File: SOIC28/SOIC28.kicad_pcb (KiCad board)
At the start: 2 copper layers, 23.1 x 35.8 mm, 7 parts, among them J1 Conn_01x14, J2 Conn_02x14_Counter_Clockwise, J3 Conn_01x14, J4 Conn_02x14_Counter_Clockwise

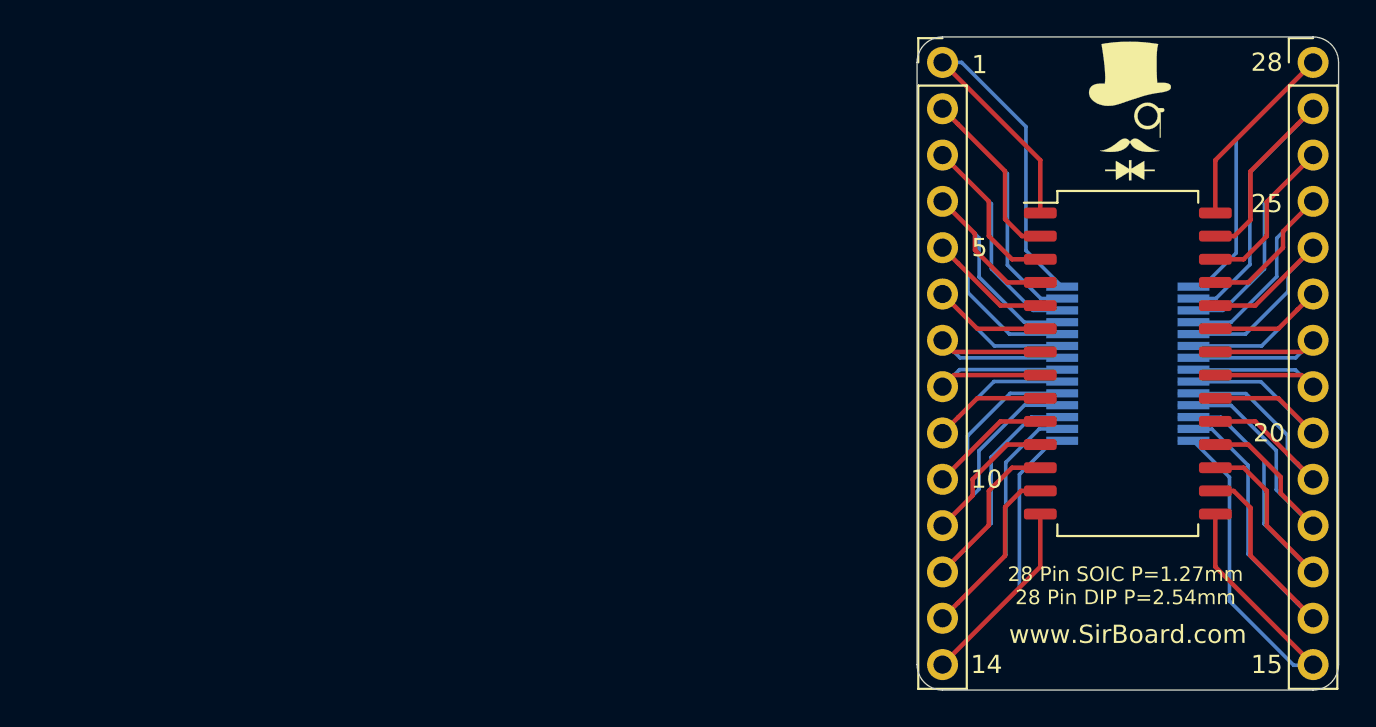
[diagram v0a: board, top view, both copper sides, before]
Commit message: Silkscreens and sizes updated
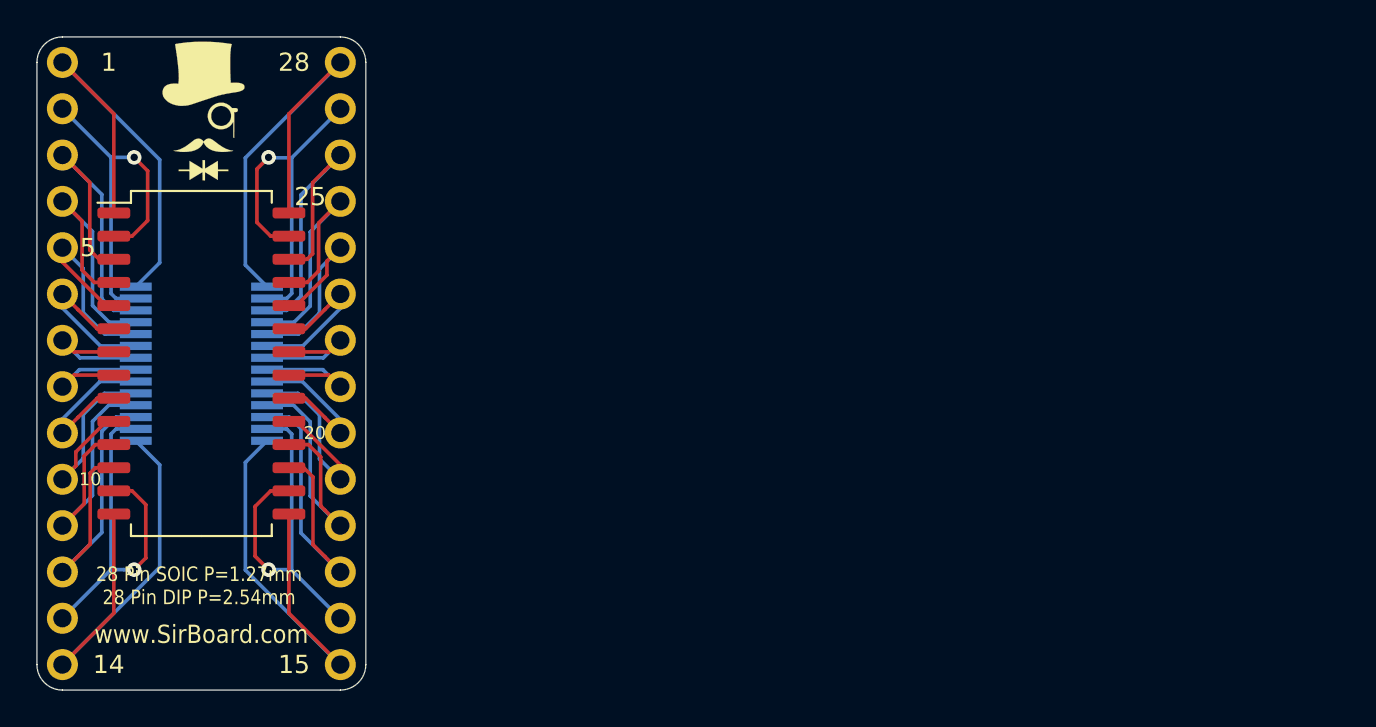
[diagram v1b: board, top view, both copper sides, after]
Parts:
- J1, J3: moved to B.Cu
- moved J3 53.3 mm to (154.9, 105.4), turned to 180 degrees
- moved G*** 50.8 mm to (147.3, 113.7)
- moved G*** 50.8 mm to (147.4, 108.1)
- moved G*** 50.8 mm to (147.3, 133.7)
- moved J2 50.8 mm to (147.3, 121.9)
- moved J4 50.8 mm to (147.3, 121.9)
- moved J1 48.3 mm to (139.7, 105.4), turned to 180 degrees
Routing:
- net Net-(J2-Pad22): track 13.3 -> 7.49 mm
- net Net-(J2-Pad21): track 13.3 -> 7.50 mm
- net Net-(J1-Pad7): track 13.3 -> 7.50 mm
- net Net-(J1-Pad8): track 13.3 -> 7.49 mm
- net Net-(J2-Pad20): track 14.6 -> 9.26 mm
- net Net-(J2-Pad23): track 14.6 -> 9.24 mm
- net Net-(J1-Pad9): track 14.6 -> 9.24 mm
- net Net-(J1-Pad6): track 14.6 -> 9.26 mm
- net Net-(J2-Pad19): track 16.6 -> 12.0 mm
- net Net-(J1-Pad5): track 16.6 -> 12.0 mm
- net Net-(J1-Pad13): track 24.4 -> 19.8 mm, vias 0 -> 1
- net Net-(J2-Pad24): track 16.5 -> 12.0 mm
- net Net-(J1-Pad10): track 16.5 -> 12.0 mm
- net Net-(J2-Pad27): track 24.4 -> 19.9 mm, vias 0 -> 1
- net Net-(J1-Pad2): track 24.4 -> 19.9 mm, vias 0 -> 1
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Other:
- board size 23.1 x 35.8 mm -> 18 x 35.8 mm

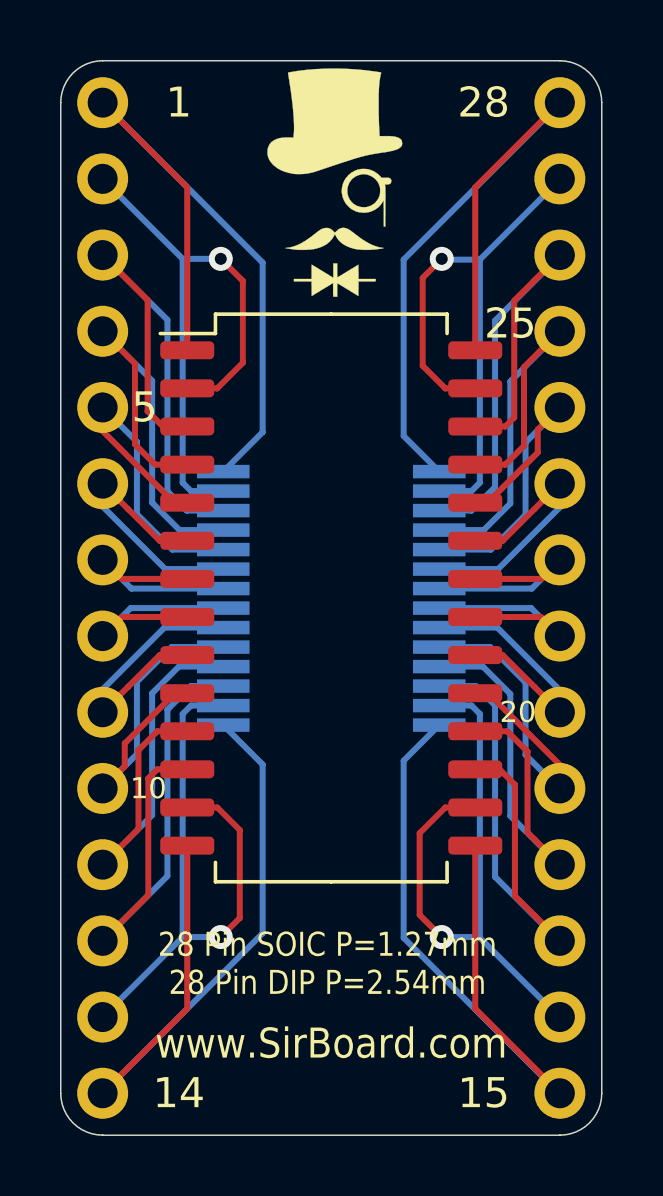
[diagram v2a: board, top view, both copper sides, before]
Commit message: Pin Numbering edited
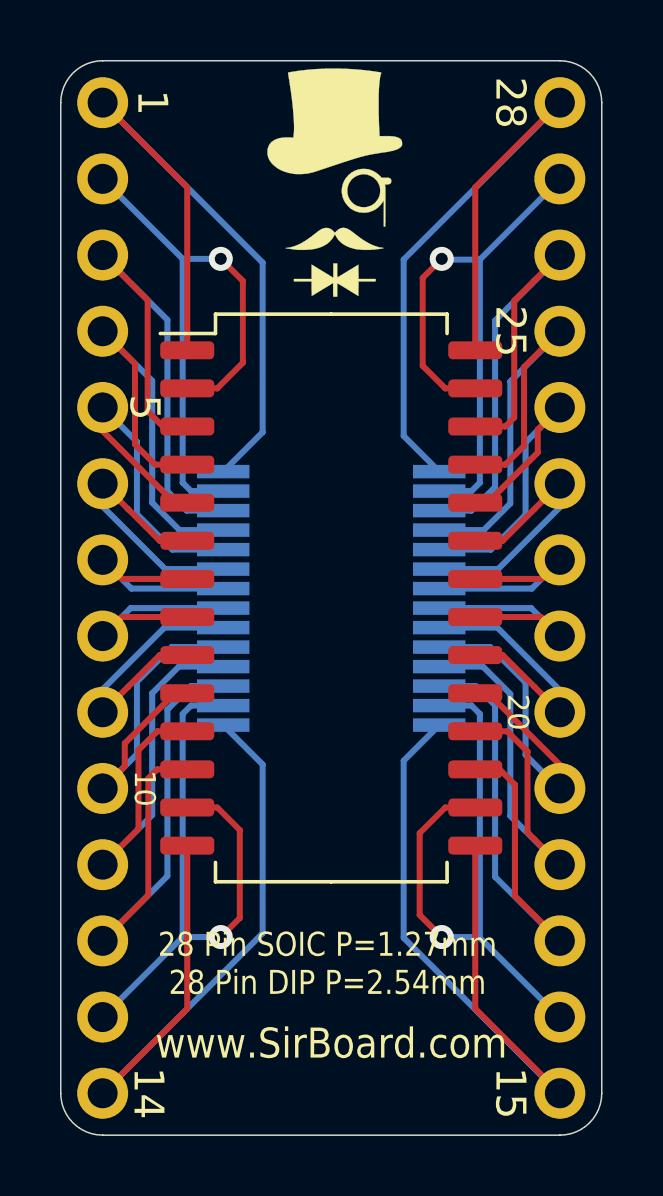
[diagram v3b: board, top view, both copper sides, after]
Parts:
- J1, J3: moved to F.Cu
- turned J1 to 0 degrees
- turned J3 to 0 degrees

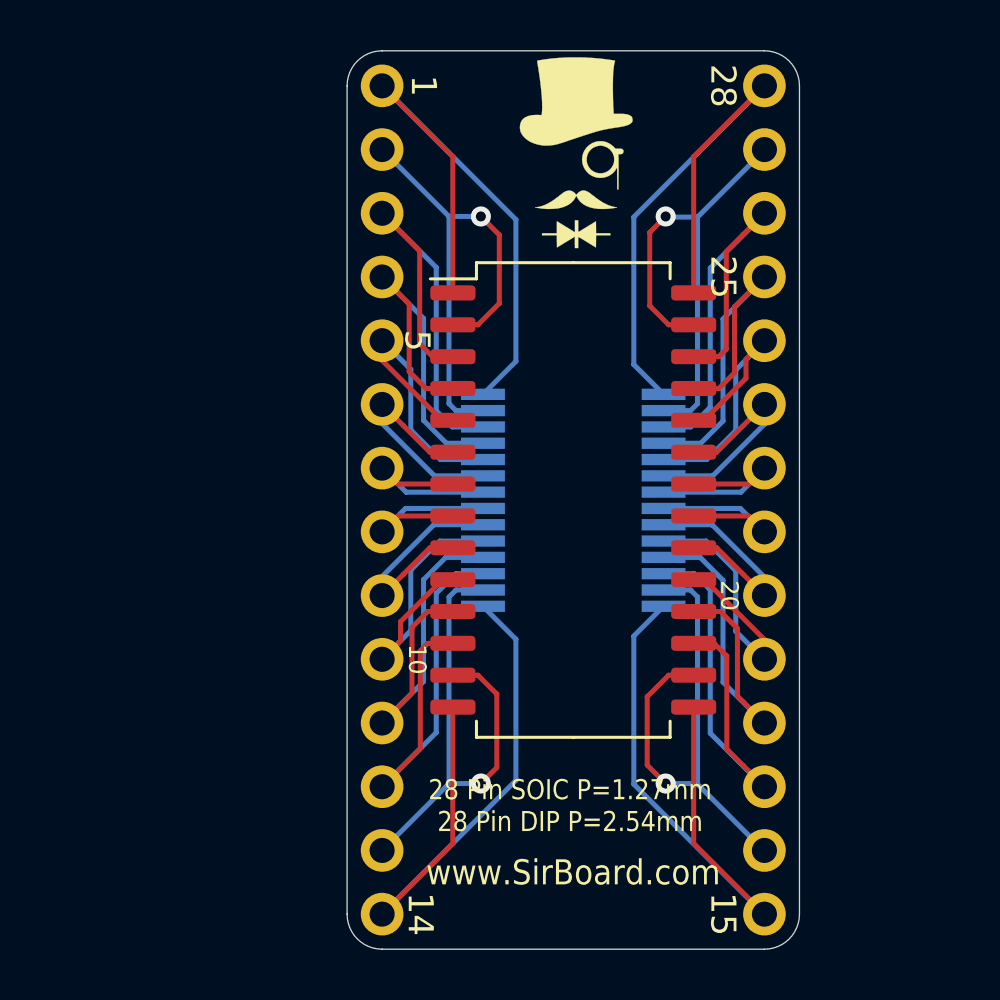
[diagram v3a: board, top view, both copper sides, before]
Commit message: Numbering Orientation Edited
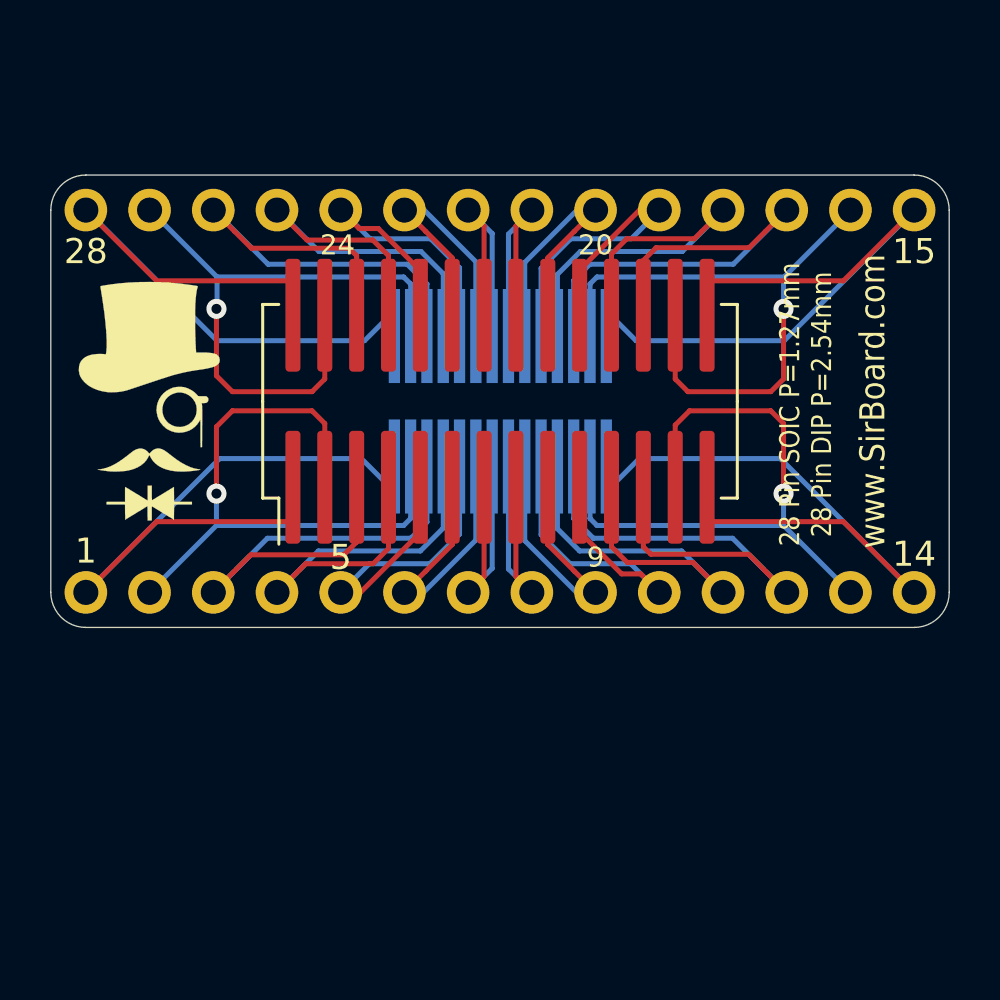
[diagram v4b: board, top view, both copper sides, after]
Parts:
- removed the G*** at (147.4, 108.1)
- removed the G*** at (147.3, 133.7)
- added G***: LOGO, logo:logo94x134, B.Cu at (157.2, 118.0)
- added G***: LOGO, logo:logo94x134, F.Cu at (130.4, 118.0)
- J1, J3: moved to B.Cu
- moved J3 27.5 mm to (127.9, 110.4), turned to 270 degrees
- moved J1 23.4 mm to (127.9, 125.6), turned to 270 degrees
- moved G*** 12.0 mm to (136.1, 118.0), turned to 90 degrees
- moved J4 4.90 mm to (144.4, 118.0), turned to 90 degrees
- moved J2 4.90 mm to (144.4, 118.0), turned to 90 degrees
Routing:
- net Net-(J1-Pad13): track 19.8 -> 25.4 mm
- net Net-(J2-Pad27): track 19.9 -> 25.3 mm
- net Net-(J2-Pad16): track 20.0 -> 25.4 mm
- net Net-(J1-Pad2): track 19.9 -> 25.3 mm
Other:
- board size 18 x 35.8 mm -> 35.8 x 18 mm
- board text added: "24"
- board text added: "9"
- board text removed: "10"
- board text removed: "25"

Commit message: Silkscreen Edits
Dimensions moved to Drawings Layer
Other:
- rule pad_to_mask_clearance: 0.051 -> 0
- rule solder_mask_min_width: 0.25 -> 0.1
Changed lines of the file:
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@@
     (38 B.Mask user)
     (39 F.Mask user)
-    (40 Dwgs.User user hide)
+    (40 Dwgs.User user)
     (41 Cmts.User user hide)
     (42 Eco1.User user hide)
@@
     (pad_size 1.7 1.7)
     (pad_drill 1)
-    (pad_to_mask_clearance 0.051)
-    (solder_mask_min_width 0.25)
+    (pad_to_mask_clearance 0)
+    (solder_mask_min_width 0.1)
     (aux_axis_origin 0 0)
     (visible_elements 7FFFFFFF)
     (pcbplotparams
-      (layerselection 0x010fc_ffffffff)
+      (layerselection 0x010f0_ffffffff)
       (usegerberextensions false)
       (usegerberattributes false)
@@
       (viasonmask false)
       (mode 1)
-      (useauxorigin false)
+      (useauxorigin true)
       (hpglpennumber 1)
       (hpglpenspeed 20)
@@
       (psa4output false)
       (plotreference true)
-      (plotvalue true)
+      (plotvalue false)
       (plotinvisibletext false)
       (padsonsilk false)
@@
       (outputformat 1)
       (mirror false)
-      (drillshape 1)
+      (drillshape 0)
       (scaleselection 1)
-      (outputdirectory ""))
+      (outputdirectory "../../Gerbers/SOIC28/"))
   )
   (net 0 "")
@@
       (xy -1.525562 0.880297)) (layer B.SilkS) (width 0.01))
   )
-  (dimension 33.02 (width 0.15) (layer F.SilkS)
-    (gr_text "33.020 mm" (at 144.399 105.634) (layer F.SilkS)
+  (dimension 33.02 (width 0.15) (layer Dwgs.User)
+    (gr_text "33.020 mm" (at 144.399 105.634) (layer Dwgs.User)
       (effects (font (size 1 1) (thickness 0.15)) hide)
     )
@@
     (arrow2b (pts (xy 127.889 106.934) (xy 129.015504 106.347579)))
   )
-  (dimension 35.814 (width 0.15) (layer F.SilkS)
-    (gr_text "35.814 mm" (at 144.399 102.713) (layer F.SilkS)
+  (dimension 35.814 (width 0.15) (layer Dwgs.User)
+    (gr_text "35.814 mm" (at 144.399 102.713) (layer Dwgs.User)
       (effects (font (size 1 1) (thickness 0.15)) hide)
     )
@@
     (arrow2b (pts (xy 126.492 104.013) (xy 127.618504 103.426579)))
   )
-  (dimension 15.24 (width 0.15) (layer F.SilkS)
-    (gr_text "15.240 mm" (at 123.287 117.983 90) (layer F.SilkS)
+  (dimension 15.24 (width 0.15) (layer Dwgs.User)
+    (gr_text "15.240 mm" (at 123.287 117.983 90) (layer Dwgs.User)
       (effects (font (size 1 1) (thickness 0.15)) hide)
     )
@@
     (arrow2b (pts (xy 124.587 125.603) (xy 124.000579 124.476496)))
   )
-  (dimension 18.034 (width 0.15) (layer F.SilkS)
-    (gr_text "18.034 mm" (at 120.239 117.983 90) (layer F.SilkS)
+  (dimension 18.034 (width 0.15) (layer Dwgs.User)
+    (gr_text "18.034 mm" (at 120.239 117.983 90) (layer Dwgs.User)
       (effects (font (size 1 1) (thickness 0.15)) hide)
     )

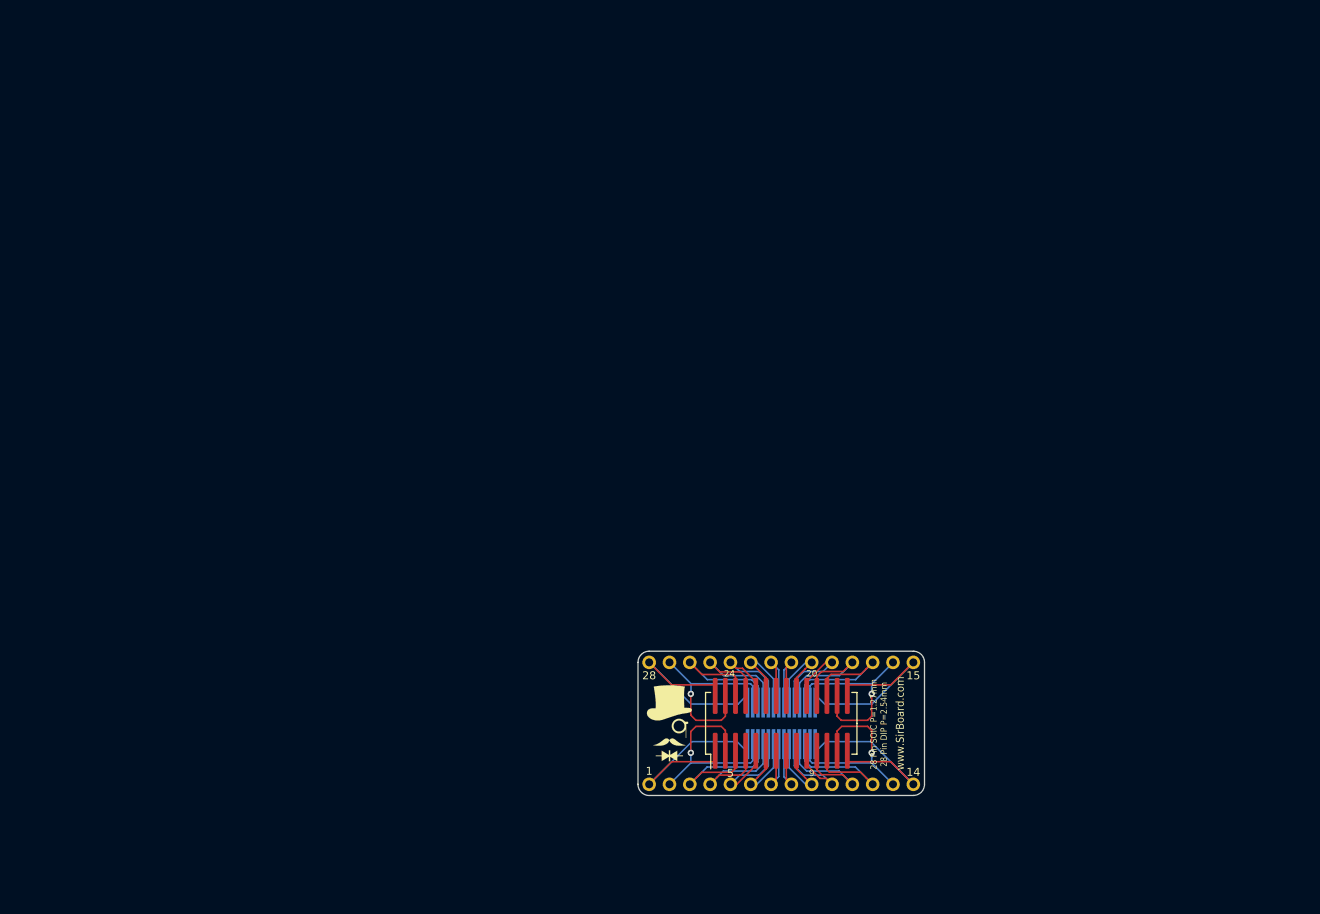
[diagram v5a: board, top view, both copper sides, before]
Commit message: USB, SD and CR Cells Added
MicroSD, MicroUSB, MiniUSB, USB-C, CR1220, CR2032 added as well as all schematics page sizes optimised
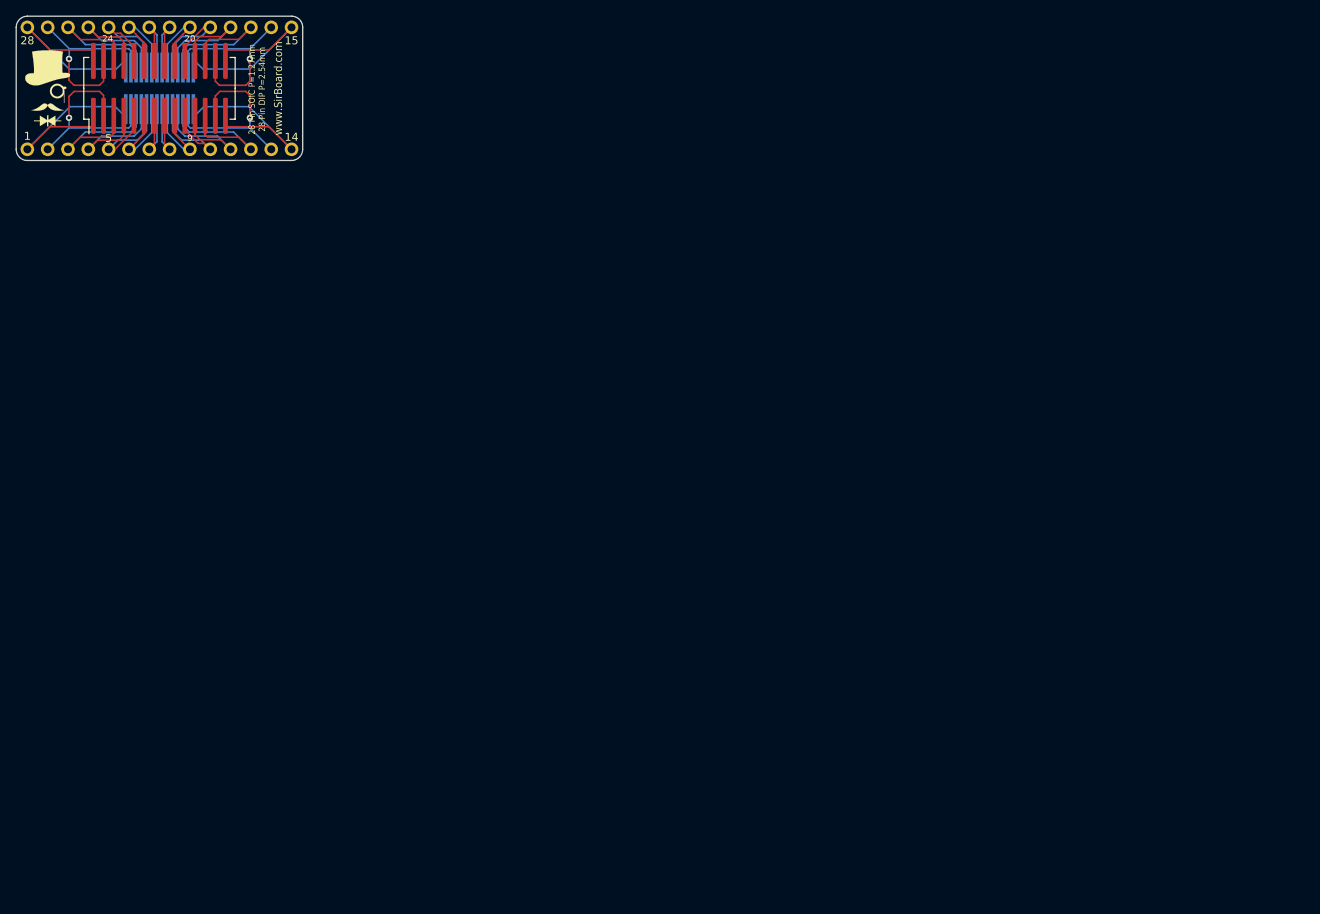
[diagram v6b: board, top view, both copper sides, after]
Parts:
- moved G*** 111.1 mm to (79.5, 38.6)
- moved G*** 111.1 mm to (52.7, 38.6)
- moved G*** 111.1 mm to (58.4, 38.6)
- moved J2 111.1 mm to (66.7, 38.6)
- moved J1 111.1 mm to (50.2, 46.2)
- moved J3 111.1 mm to (50.2, 31.0)
- moved J4 111.1 mm to (66.7, 38.6)
